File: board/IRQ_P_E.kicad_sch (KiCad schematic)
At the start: 18 parts, among them IC5 74LS219, IC6 74LS219, IC7 74LS219, IC8 74LS219, U17 74LS148, U18 74LS148, U44 74F00, U45 74F157

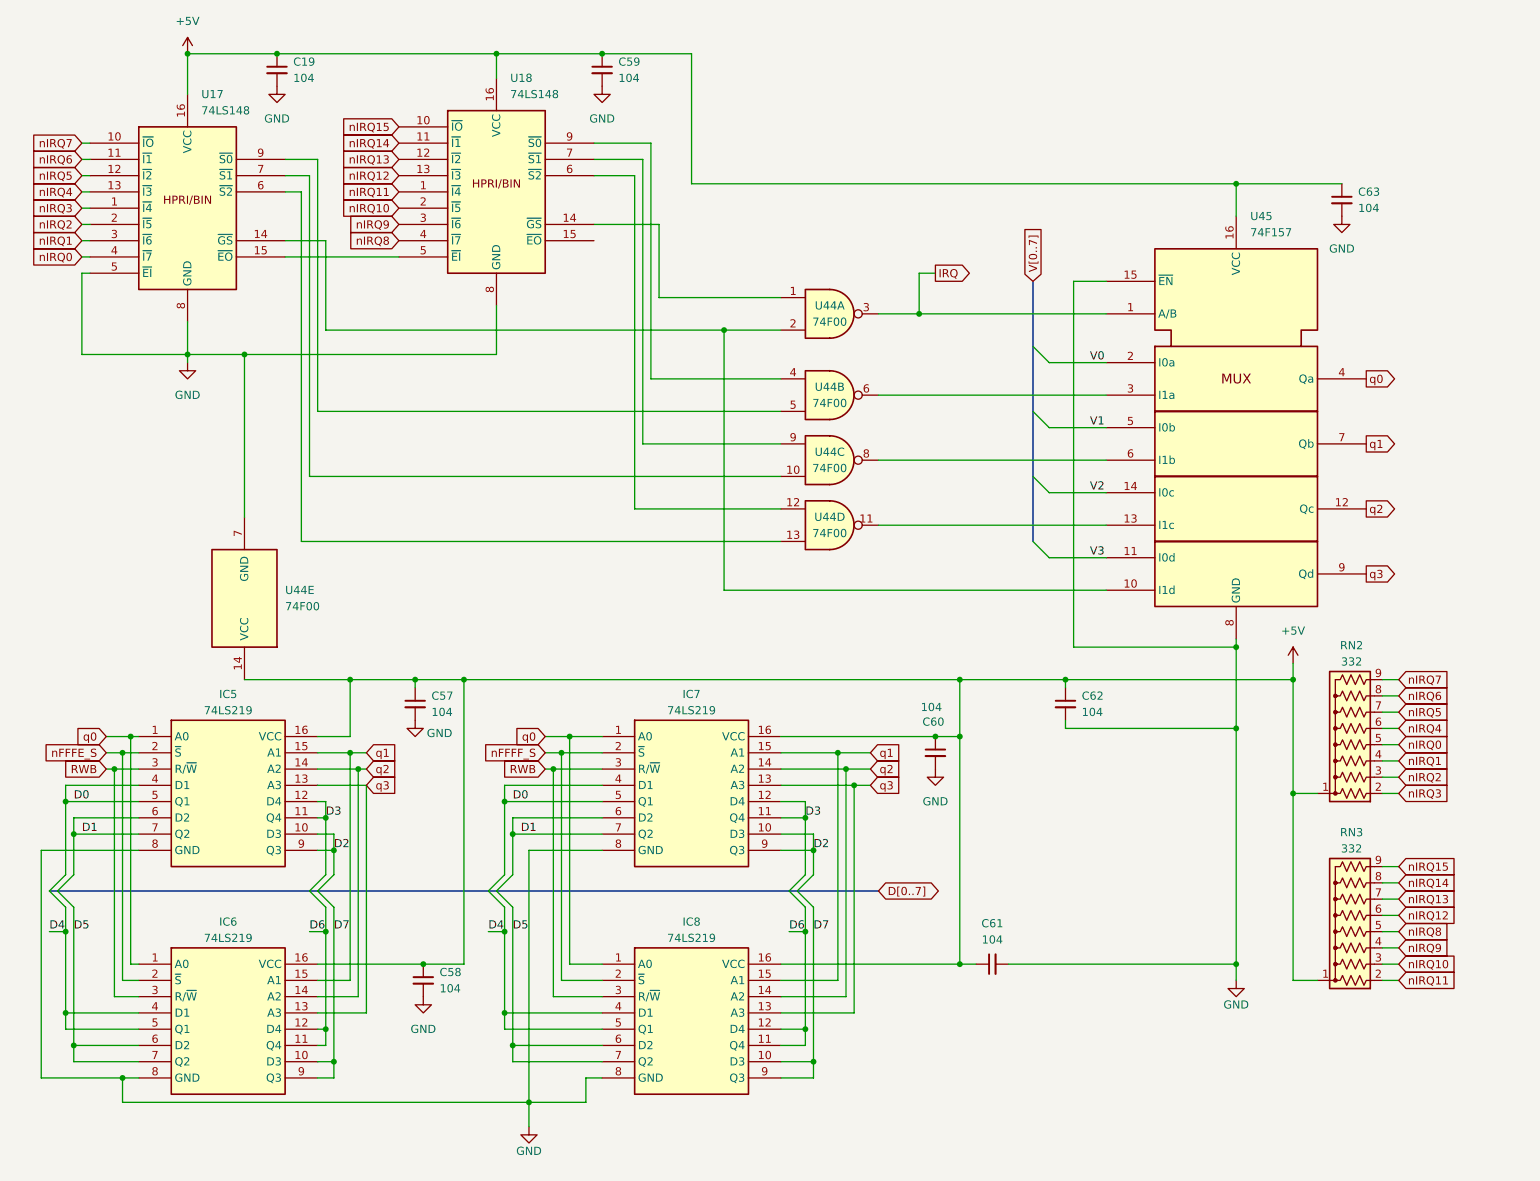
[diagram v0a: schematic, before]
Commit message: V2.0 changes with new S register and simplified logic
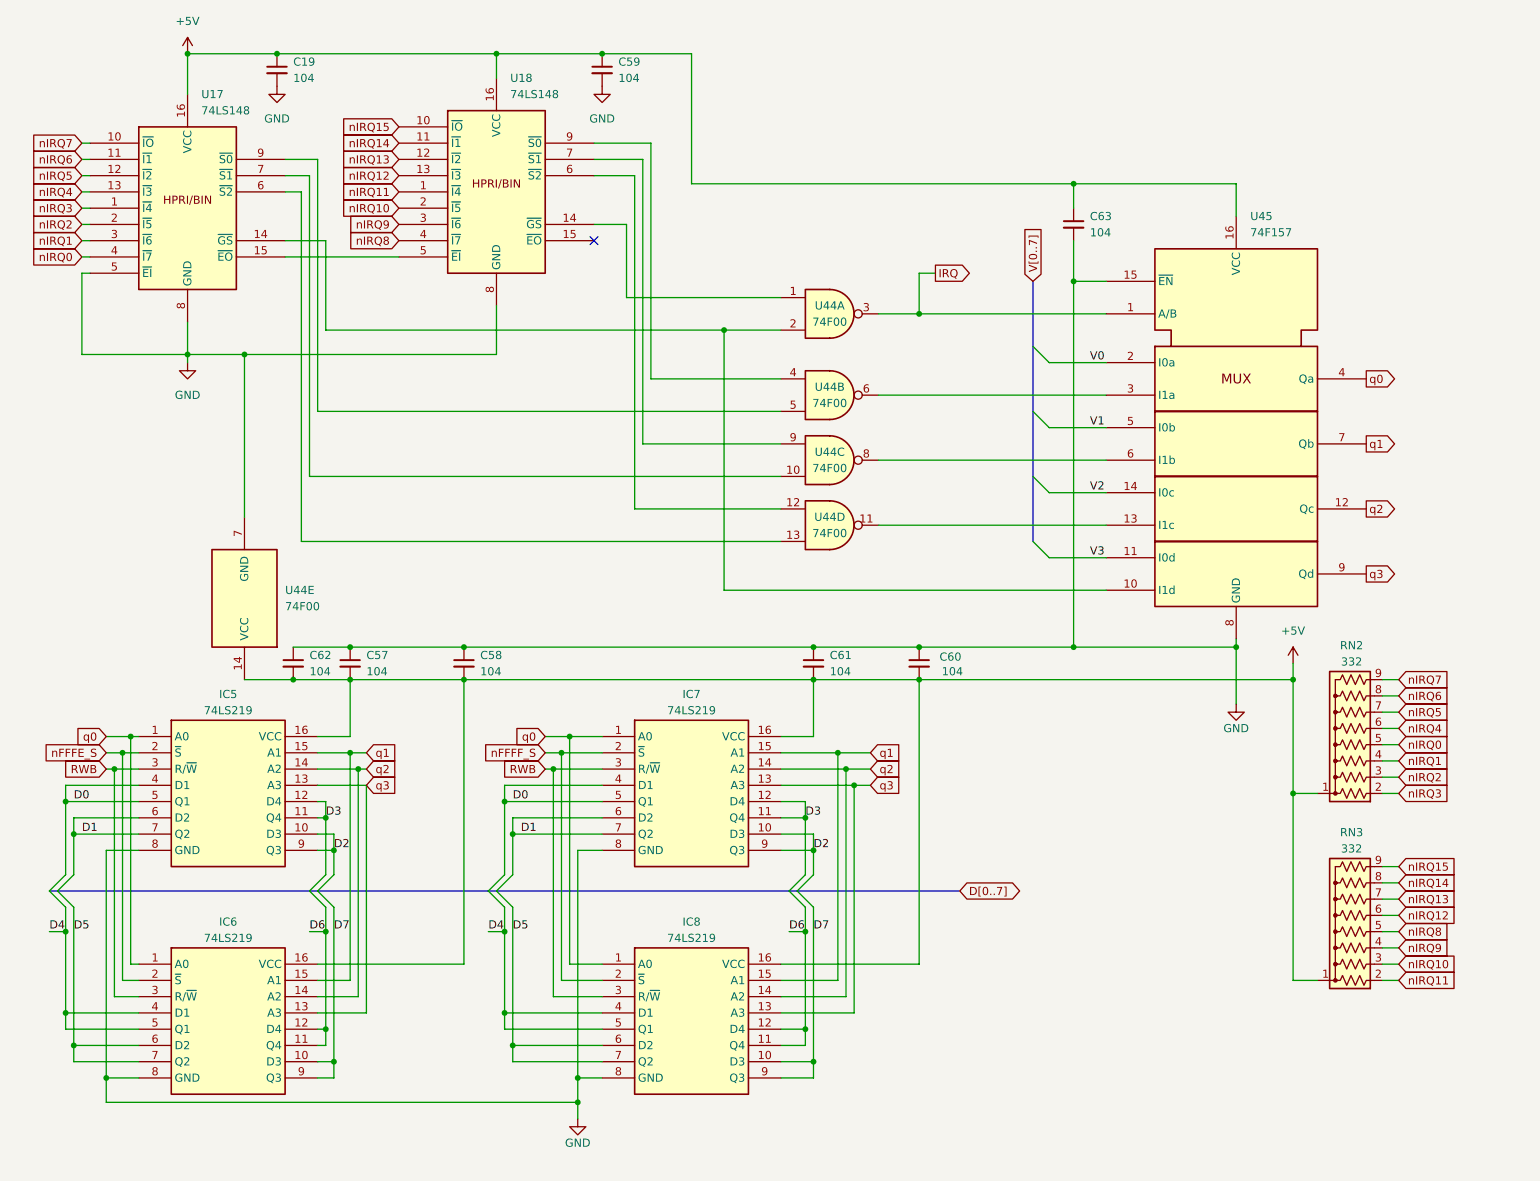
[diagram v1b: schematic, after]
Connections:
- net +5V: now also C57.2, C58.2, C60.2, C61.2, C62.2; no longer C57.1, C58.1, C60.1, C61.1, C62.1
- net GND: now also C57.1, C58.1, C60.1, C61.1, C62.1; no longer C57.2, C58.2, C60.2, C61.2, C62.2
- no-connect marks 0 -> 1
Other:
- moved on the sheet: C57, C58, C60, C61, C62, C63

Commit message: V2.0 updates and new hydra breakout and counter cards.
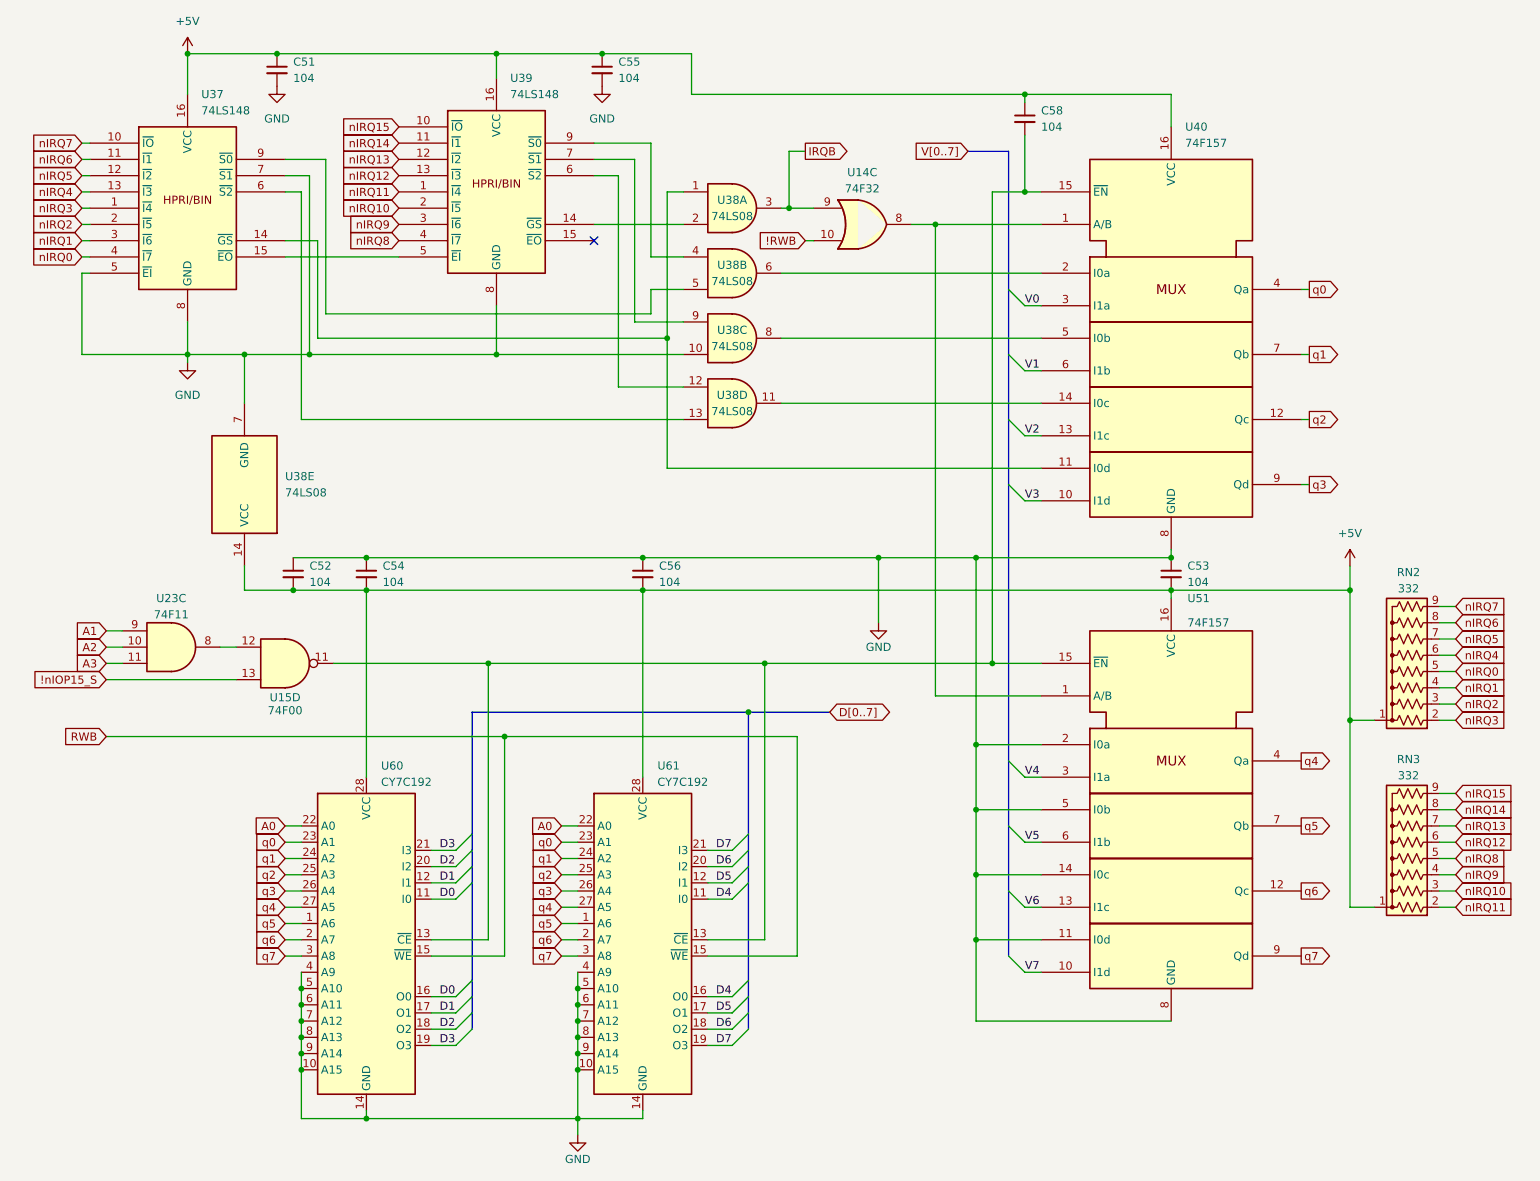
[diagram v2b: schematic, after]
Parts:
- removed C60: 104, Capacitor_THT:C_Disc_D5.0mm_W2.5mm_P5.00mm, symbol Device:C_Small
- removed IC5, IC6, IC7, IC8: 74LS219, Package_DIP:DIP-16_W7.62mm_Socket_LongPads, symbol 74xx:74LS219
- added U14: 74F32, Package_DIP:DIP-14_W7.62mm_Socket_LongPads, symbol 74xx:74LS32
- added U15: 74F00, Package_DIP:DIP-14_W7.62mm_Socket_LongPads, symbol 74xx:74LS00
- added U23: 74F11, Package_DIP:DIP-14_W7.62mm_Socket_LongPads, symbol 74xx:74LS11
- added U51: 74F157, Package_DIP:DIP-16_W7.62mm_Socket_LongPads, symbol 74xx_IEEE:74157
- added U60, U61: CY7C192, Package_DIP:DIP-28_W15.24mm_Socket_LongPads, symbol 65XX:6551
- U38: renamed from U44; value 74F00 -> 74LS08; symbol 74xx:74LS00 -> 74xx:74LS08
- renumbered C19 to C51, C62 to C52, C57 to C53, C58 to C54, C59 to C55, C61 to C56, C63 to C58, U17 to U37, U18 to U39, U45 to U40
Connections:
- net +5V: now also U51.16 (VCC), U60.28 (VCC), U61.28 (VCC)
- net D0: now also U60.11 (I0), U60.16 (O0)
- net D1: now also U60.12 (I1), U60.17 (O1)
- net D2: now also U60.18 (O2), U60.20 (I2)
- net D3: now also U60.19 (O3), U60.21 (I3)
- net D4: now also U61.11 (I0), U61.16 (O0)
- net D5: now also U61.12 (I1), U61.17 (O1)
- net D6: now also U61.18 (O2), U61.20 (I2)
- net D7: now also U61.19 (O3), U61.21 (I3)
- net GND: now also U37.7 (~{S1}), U38.10, U51.11 (I0d), U51.14 (I0c), U51.2 (I0a), U51.5 (I0b), U51.8 (GND), U60.10 (A15), U60.14 (GND), U60.4 (A9), U60.5 (A10), U60.6 (A11), U60.7 (A12), U60.8 (A13), U60.9 (A14), U61.10 (A15), U61.14 (GND), U61.4 (A9), U61.5 (A10), U61.6 (A11), U61.7 (A12), U61.8 (A13), U61.9 (A14); no longer C58.2, U40.15 (~{EN})
- net RWB: now also U60.15 (~{WE}), U61.15 (~{WE})
- net V0: now also U40.3 (I1a); no longer U40.2 (I0a)
- net V1: now also U40.6 (I1b); no longer U40.5 (I0b)
- net V2: now also U40.13 (I1c); no longer U40.14 (I0c)
- net V3: now also U40.10 (I1d); no longer U40.11 (I0d)
- net q0: now also U60.23 (A1), U61.23 (A1)
- net q1: now also U60.24 (A2), U61.24 (A2)
- net q2: now also U60.25 (A3), U61.25 (A3)
- net q3: now also U60.26 (A4), U61.26 (A4)
- net at U38.6: now also U40.2 (I0a); no longer U40.3 (I1a)
- net at U38.8: now also U40.5 (I0b); no longer U40.6 (I1b)
- net at U38.1: now also U37.14 (~{GS}), U40.11 (I0d); no longer U39.14 (~{GS})
- net at U38.11: now also U40.14 (I0c); no longer U40.13 (I1c)
- net IRQ: no longer names the net of U40.1 (A/B)
- net IRQ: now also U14.8, U51.1 (A/B); no longer U38.3
- new net: C58.2, U15.11, U40.15 (~{EN}), U51.15 (~{EN}), U60.13 (~{CE}), U61.13 (~{CE})
- new net: U38.2, U39.14 (~{GS})
- new net: U15.12, U23.8
- new net !RWB: U14.10
- new net !nIOP15_S: U15.13
- new net A0: U60.22 (A0), U61.22 (A0)
- new net A1: U23.9
- new net A2: U23.10
- new net A3: U23.11
- new net IRQB: U14.9, U38.3
- new net V4: U51.3 (I1a)
- new net V5: U51.6 (I1b)
- new net V6: U51.13 (I1c)
- new net V7: U51.10 (I1d)
- new net q4: U51.4 (Qa), U60.27 (A5), U61.27 (A5)
- new net q5: U51.7 (Qb), U60.1 (A6), U61.1 (A6)
- new net q6: U51.12 (Qc), U60.2 (A7), U61.2 (A7)
- new net q7: U51.9 (Qd), U60.3 (A8), U61.3 (A8)
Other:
- title: IRQ Priority Logic and Vector Memory -> ZeroPage $00/$01 Mirror Memory and RAM/ROM Bank Logic
- moved on the sheet: C52, C53, C54, C56, C58, RN2, RN3, U38E, U40
